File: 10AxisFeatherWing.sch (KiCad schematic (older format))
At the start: 24 parts, among them J1 feather long, J2 feather short, J3 INT, J4 feather long, J5 feather short, SW1 SW_Push_Dual, U1 BNO055, U2 BME280, Y1 32.768kHz

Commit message: Updated features
Replaced NRESET with pin instead of a button, Added silk text
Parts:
- removed R3: 10K, Resistor_SMD:R_0603_1608Metric, symbol Device:R_Small
- removed SW1: SW_Push_Dual, Button_Switch_SMD:SW_Push_1P1T_NO_CK_KMR2, symbol Switch:SW_Push_Dual
- added J6: NRESET, Connector_Wire:SolderWirePad_1x01_Drill0.8mm, symbol Connector_Generic:Conn_01x01
- J3: renamed from J4; footprint Connector_PinHeader_2.54mm:PinHeader_1x16_P2.54mm_Vertical -> Connector_PinSocket_2.54mm:PinSocket_1x16_P2.54mm_Vertical
- J4: renamed from J5; footprint Connector_PinHeader_2.54mm:PinHeader_1x12_P2.54mm_Vertical -> Connector_PinSocket_2.54mm:PinSocket_1x12_P2.54mm_Vertical
- J5: renamed from J3; footprint Connector_PinSocket_1.27mm:PinSocket_1x01_P1.27mm_Vertical -> Connector_Wire:SolderWirePad_1x01_Drill0.8mm
- renumbered C4 to C1, C5 to C2, C6 to C3, C7 to C4, C8 to C5, C2 to C6, C1 to C7, C3 to C8, R4 to R3, R5 to R4
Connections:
- net NRESET: now also J6.1 (Pin_1)
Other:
- moved on the sheet: J5, R1, R2

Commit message: Minor format fix
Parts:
- added H1, H2, H3, H4: MountingHole, MountingHole:MountingHole_2.7mm_M2.5, symbol Mechanical:MountingHole
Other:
- moved on the sheet: J5, J6
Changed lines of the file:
@@
 L Connector_Generic:Conn_01x01 J5
 U 1 1 5E233B4E
-P 10000 5500
-F 0 "J5" H 10080 5542 50  0000 L CNN
-F 1 "INT" H 10080 5451 50  0000 L CNN
-F 2 "Connector_Wire:SolderWirePad_1x01_Drill0.8mm" H 10000 5500 50  0001 C CNN
-F 3 "~" H 10000 5500 50  0001 C CNN
-	1    10000 5500
+P 10000 4800
+F 0 "J5" H 10080 4842 50  0000 L CNN
+F 1 "INT" H 10080 4751 50  0000 L CNN
+F 2 "Connector_Wire:SolderWirePad_1x01_Drill0.8mm" H 10000 4800 50  0001 C CNN
+F 3 "~" H 10000 4800 50  0001 C CNN
+	1    10000 4800
 	1    0    0    -1
 $EndComp
-Text Label 9000 5500 0    50   ~ 0
+Text Label 9000 4800 0    50   ~ 0
 INT
 Wire Wire Line
@@
 Wire Notes Line
 	6200 500  6200 8000
-Text Label 9000 6000 0    50   ~ 0
+Text Label 9000 5300 0    50   ~ 0
 NRESET
 $Comp
 L Connector_Generic:Conn_01x01 J6
 U 1 1 5E15A9A2
-P 10000 6000
-F 0 "J6" H 10080 6042 50  0000 L CNN
-F 1 "NRESET" H 10080 5951 50  0000 L CNN
-F 2 "Connector_Wire:SolderWirePad_1x01_Drill0.8mm" H 10000 6000 50  0001 C CNN
-F 3 "~" H 10000 6000 50  0001 C CNN
-	1    10000 6000
+P 10000 5300
+F 0 "J6" H 10080 5342 50  0000 L CNN
+F 1 "NRESET" H 10080 5251 50  0000 L CNN
+F 2 "Connector_Wire:SolderWirePad_1x01_Drill0.8mm" H 10000 5300 50  0001 C CNN
+F 3 "~" H 10000 5300 50  0001 C CNN
+	1    10000 5300
 	1    0    0    -1
 $EndComp
 Wire Wire Line
-	9000 5500 9800 5500
+	9000 4800 9800 4800
 Wire Wire Line
-	9000 6000 9800 6000
+	9000 5300 9800 5300
 Wire Wire Line
 	6500 2000 7750 2000
@@
 Wire Wire Line
 	7250 1500 7250 1350
+$Comp
+L Mechanical:MountingHole H1
+U 1 1 5E165FBB
+P 9250 5750
+F 0 "H1" H 9350 5796 50  0000 L CNN
+F 1 "MountingHole" H 9350 5705 50  0000 L CNN
+F 2 "MountingHole:MountingHole_2.7mm_M2.5" H 9250 5750 50  0001 C CNN
+F 3 "~" H 9250 5750 50  0001 C CNN
+	1    9250 5750
+	1    0    0    -1
+$EndComp
+$Comp
+L Mechanical:MountingHole H2
+U 1 1 5E16676B
+P 9250 6000
+F 0 "H2" H 9350 6046 50  0000 L CNN
+F 1 "MountingHole" H 9350 5955 50  0000 L CNN
+F 2 "MountingHole:MountingHole_2.7mm_M2.5" H 9250 6000 50  0001 C CNN
+F 3 "~" H 9250 6000 50  0001 C CNN
+	1    9250 6000
+	1    0    0    -1
+$EndComp
+$Comp
+L Mechanical:MountingHole H3
+U 1 1 5E166D96
+P 9250 6250
+F 0 "H3" H 9350 6296 50  0000 L CNN
+F 1 "MountingHole" H 9350 6205 50  0000 L CNN
+F 2 "MountingHole:MountingHole_2.7mm_M2.5" H 9250 6250 50  0001 C CNN
+F 3 "~" H 9250 6250 50  0001 C CNN
+	1    9250 6250
+	1    0    0    -1
+$EndComp
+$Comp
+L Mechanical:MountingHole H4
+U 1 1 5E16742A
+P 9250 6500
+F 0 "H4" H 9350 6546 50  0000 L CNN
+F 1 "MountingHole" H 9350 6455 50  0000 L CNN
+F 2 "MountingHole:MountingHole_2.7mm_M2.5" H 9250 6500 50  0001 C CNN
+F 3 "~" H 9250 6500 50  0001 C CNN
+	1    9250 6500
+	1    0    0    -1
+$EndComp
+Wire Notes Line
+	8350 5500 10500 5500
 $EndSCHEMATC

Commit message: Increased trace width
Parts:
- added R3: 10K, Resistor_SMD:R_0603_1608Metric, symbol Device:R_Small
- renumbered R3 to R4, R4 to R5
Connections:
- net +3V3: now also R3.1
- net NRESET: now also R3.2
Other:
- moved on the sheet: R2
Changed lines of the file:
@@
 $EndComp
 $Comp
-L power:GND #PWR06
+L power:GND #PWR07
 U 1 1 5D3787E4
 P 8550 1300
-F 0 "#PWR06" H 8550 1050 50  0001 C CNN
+F 0 "#PWR07" H 8550 1050 50  0001 C CNN
 F 1 "GND" H 8555 1127 50  0000 C CNN
 F 2 "" H 8550 1300 50  0001 C CNN
@@
 $EndComp
 $Comp
-L power:+3.3V #PWR04
+L power:+3.3V #PWR05
 U 1 1 5E0B811E
 P 2900 1150
-F 0 "#PWR04" H 2900 1000 50  0001 C CNN
+F 0 "#PWR05" H 2900 1000 50  0001 C CNN
 F 1 "+3.3V" H 2915 1323 50  0000 C CNN
 F 2 "" H 2900 1150 50  0001 C CNN
@@
 $EndComp
 $Comp
-L power:+3.3V #PWR05
+L power:+3.3V #PWR06
 U 1 1 5E0B916F
 P 3100 1150
-F 0 "#PWR05" H 3100 1000 50  0001 C CNN
+F 0 "#PWR06" H 3100 1000 50  0001 C CNN
 F 1 "+3.3V" H 3115 1323 50  0000 C CNN
 F 2 "" H 3100 1150 50  0001 C CNN
@@
 $EndComp
 $Comp
-L power:GND #PWR010
+L power:GND #PWR011
 U 1 1 5E0B93DE
 P 3000 3900
-F 0 "#PWR010" H 3000 3650 50  0001 C CNN
+F 0 "#PWR011" H 3000 3650 50  0001 C CNN
 F 1 "GND" H 3005 3727 50  0000 C CNN
 F 2 "" H 3000 3900 50  0001 C CNN
@@
 	4500 3300 4500 3400
 $Comp
-L power:+3.3V #PWR013
+L power:+3.3V #PWR014
 U 1 1 5E0F5D23
 P 2900 5250
-F 0 "#PWR013" H 2900 5100 50  0001 C CNN
+F 0 "#PWR014" H 2900 5100 50  0001 C CNN
 F 1 "+3.3V" H 2915 5423 50  0000 C CNN
 F 2 "" H 2900 5250 50  0001 C CNN
@@
 $EndComp
 $Comp
-L power:+3.3V #PWR014
+L power:+3.3V #PWR015
 U 1 1 5E0F8609
 P 3100 5250
-F 0 "#PWR014" H 3100 5100 50  0001 C CNN
+F 0 "#PWR015" H 3100 5100 50  0001 C CNN
 F 1 "+3.3V" H 3115 5423 50  0000 C CNN
 F 2 "" H 3100 5250 50  0001 C CNN
@@
 $EndComp
 $Comp
-L power:GND #PWR016
+L power:GND #PWR017
 U 1 1 5E0F88FA
 P 3000 7150
-F 0 "#PWR016" H 3000 6900 50  0001 C CNN
+F 0 "#PWR017" H 3000 6900 50  0001 C CNN
 F 1 "GND" H 3005 6977 50  0000 C CNN
 F 2 "" H 3000 7150 50  0001 C CNN
@@
 	9700 4450 9950 4450
 $Comp
-L power:+3.3V #PWR07
+L power:+3.3V #PWR08
 U 1 1 5E16B6E2
 P 8550 2950
-F 0 "#PWR07" H 8550 2800 50  0001 C CNN
+F 0 "#PWR08" H 8550 2800 50  0001 C CNN
 F 1 "+3.3V" H 8565 3123 50  0000 C CNN
 F 2 "" H 8550 2950 50  0001 C CNN
@@
 $EndComp
 $Comp
-L power:GND #PWR09
+L power:GND #PWR010
 U 1 1 5E16B6EC
 P 8550 3350
-F 0 "#PWR09" H 8550 3100 50  0001 C CNN
+F 0 "#PWR010" H 8550 3100 50  0001 C CNN
 F 1 "GND" H 8555 3177 50  0000 C CNN
 F 2 "" H 8550 3350 50  0001 C CNN
@@
 L Device:R_Small R2
 U 1 1 5E1917EB
-P 7750 1250
-F 0 "R2" H 7809 1296 50  0000 L CNN
-F 1 "10K" H 7809 1205 50  0000 L CNN
-F 2 "Resistor_SMD:R_0603_1608Metric" H 7750 1250 50  0001 C CNN
-F 3 "~" H 7750 1250 50  0001 C CNN
-	1    7750 1250
+P 7500 1250
+F 0 "R2" H 7559 1296 50  0000 L CNN
+F 1 "10K" H 7559 1205 50  0000 L CNN
+F 2 "Resistor_SMD:R_0603_1608Metric" H 7500 1250 50  0001 C CNN
+F 3 "~" H 7500 1250 50  0001 C CNN
+	1    7500 1250
 	1    0    0    -1
 $EndComp
@@
 Text Label 6500 1500 0    50   ~ 0
 SDA
-Text Label 6500 2000 0    50   ~ 0
+Text Label 6500 1750 0    50   ~ 0
 SCL
 $Comp
@@
 L power:+3.3V #PWR03
 U 1 1 5E1FAD43
-P 7750 1050
-F 0 "#PWR03" H 7750 900 50  0001 C CNN
-F 1 "+3.3V" H 7765 1223 50  0000 C CNN
-F 2 "" H 7750 1050 50  0001 C CNN
-F 3 "" H 7750 1050 50  0001 C CNN
-	1    7750 1050
+P 7500 1050
+F 0 "#PWR03" H 7500 900 50  0001 C CNN
+F 1 "+3.3V" H 7515 1223 50  0000 C CNN
+F 2 "" H 7500 1050 50  0001 C CNN
+F 3 "" H 7500 1050 50  0001 C CNN
+	1    7500 1050
 	1    0    0    -1
 $EndComp
@@
 	7250 1150 7250 1050
 Wire Wire Line
-	7750 1150 7750 1050
+	7500 1150 7500 1050
 $Comp
 L Jumper:SolderJumper_2_Open JP1
@@
 $EndComp
 $Comp
-L Device:R_Small R3
+L Device:R_Small R4
 U 1 1 5E22C94C
 P 7750 3750
-F 0 "R3" V 7554 3750 50  0000 C CNN
+F 0 "R4" V 7554 3750 50  0000 C CNN
 F 1 "10K" V 7645 3750 50  0000 C CNN
 F 2 "Resistor_SMD:R_0603_1608Metric" H 7750 3750 50  0001 C CNN
@@
 $EndComp
 $Comp
-L Device:R_Small R4
+L Device:R_Small R5
 U 1 1 5E22CD6F
 P 7750 5750
-F 0 "R4" V 7554 5750 50  0000 C CNN
+F 0 "R5" V 7554 5750 50  0000 C CNN
 F 1 "10K" V 7645 5750 50  0000 C CNN
 F 2 "Resistor_SMD:R_0603_1608Metric" H 7750 5750 50  0001 C CNN
@@
 	7250 3750 7650 3750
 $Comp
-L power:+3.3V #PWR08
+L power:+3.3V #PWR09
 U 1 1 5E248530
 P 7250 3000
-F 0 "#PWR08" H 7250 2850 50  0001 C CNN
+F 0 "#PWR09" H 7250 2850 50  0001 C CNN
 F 1 "+3.3V" H 7265 3173 50  0000 C CNN
 F 2 "" H 7250 3000 50  0001 C CNN
@@
 $EndComp
 $Comp
-L power:+3.3V #PWR012
+L power:+3.3V #PWR013
 U 1 1 5E248952
 P 7250 5000
-F 0 "#PWR012" H 7250 4850 50  0001 C CNN
+F 0 "#PWR013" H 7250 4850 50  0001 C CNN
 F 1 "+3.3V" H 7265 5173 50  0000 C CNN
 F 2 "" H 7250 5000 50  0001 C CNN
@@
 	7250 5750 7650 5750
 $Comp
-L power:GND #PWR011
+L power:GND #PWR012
 U 1 1 5E263677
 P 8000 4000
-F 0 "#PWR011" H 8000 3750 50  0001 C CNN
+F 0 "#PWR012" H 8000 3750 50  0001 C CNN
 F 1 "GND" H 8005 3827 50  0000 C CNN
 F 2 "" H 8000 4000 50  0001 C CNN
@@
 $EndComp
 $Comp
-L power:GND #PWR015
+L power:GND #PWR016
 U 1 1 5E263AA5
 P 8000 6000
-F 0 "#PWR015" H 8000 5750 50  0001 C CNN
+F 0 "#PWR016" H 8000 5750 50  0001 C CNN
 F 1 "GND" H 8005 5827 50  0000 C CNN
 F 2 "" H 8000 6000 50  0001 C CNN
@@
 	9000 5300 9800 5300
 Wire Wire Line
-	6500 2000 7750 2000
-Wire Wire Line
-	7750 2000 7750 1350
+	6500 1750 7500 1750
 Wire Wire Line
 	6500 1500 7250 1500
@@
 Wire Notes Line
 	8350 5500 10500 5500
+Wire Wire Line
+	7500 1750 7500 1350
+$Comp
+L Device:R_Small R3
+U 1 1 5E1C1A5F
+P 7750 1250
+F 0 "R3" H 7809 1296 50  0000 L CNN
+F 1 "10K" H 7809 1205 50  0000 L CNN
+F 2 "Resistor_SMD:R_0603_1608Metric" H 7750 1250 50  0001 C CNN
+F 3 "~" H 7750 1250 50  0001 C CNN
+	1    7750 1250
+	1    0    0    -1
+$EndComp
+$Comp
+L power:+3.3V #PWR04
+U 1 1 5E1C1A69
+P 7750 1050
+F 0 "#PWR04" H 7750 900 50  0001 C CNN
+F 1 "+3.3V" H 7765 1223 50  0000 C CNN
+F 2 "" H 7750 1050 50  0001 C CNN
+F 3 "" H 7750 1050 50  0001 C CNN
+	1    7750 1050
+	1    0    0    -1
+$EndComp
+Wire Wire Line
+	7750 1150 7750 1050
+Text Label 6500 2000 0    50   ~ 0
+NRESET
+Wire Wire Line
+	6500 2000 7750 2000
+Wire Wire Line
+	7750 1350 7750 2000
 $EndSCHEMATC

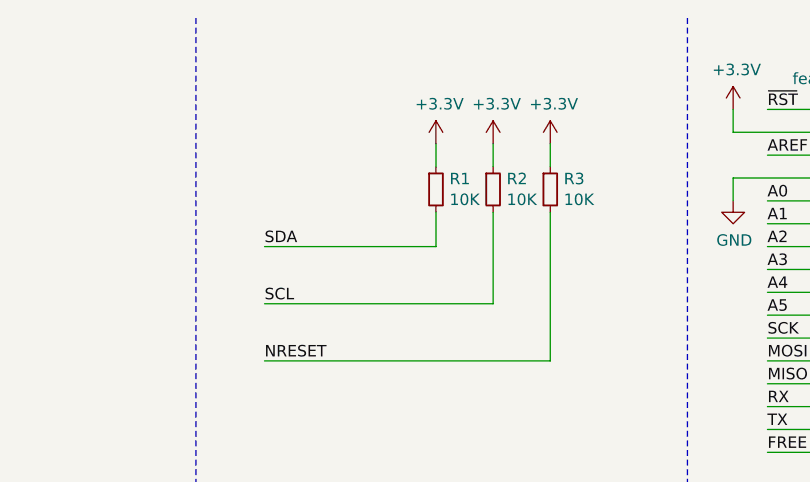
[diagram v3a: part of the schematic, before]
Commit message: I2C pull-up resistor fix
Changed I2C pull-up resistor values from 10K to 4.7K
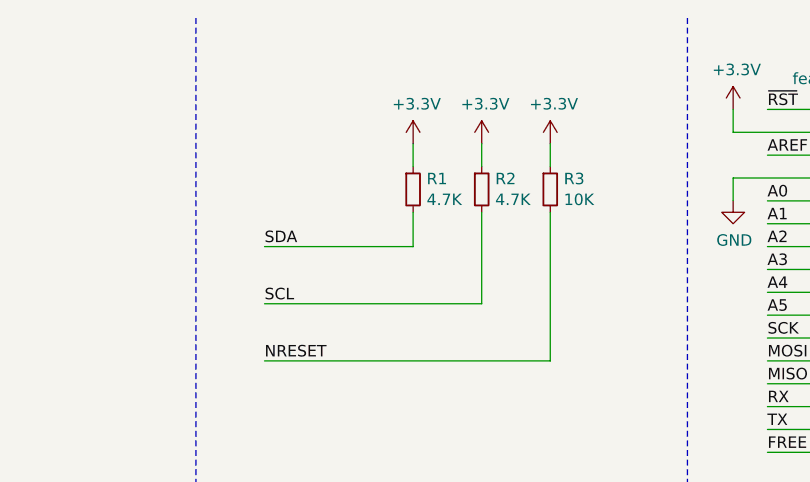
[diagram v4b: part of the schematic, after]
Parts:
- R1, R2: value 10K -> 4.7K
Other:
- moved on the sheet: R1, R2
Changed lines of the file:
@@
 	8350 500  8350 6650
-$Comp
-L Device:R_Small R1
-U 1 1 5E19106A
-P 7250 1250
-F 0 "R1" H 7309 1296 50  0000 L CNN
-F 1 "10K" H 7309 1205 50  0000 L CNN
-F 2 "Resistor_SMD:R_0603_1608Metric" H 7250 1250 50  0001 C CNN
-F 3 "~" H 7250 1250 50  0001 C CNN
-	1    7250 1250
-	1    0    0    -1
-$EndComp
 $Comp
 L Device:R_Small R2
 U 1 1 5E1917EB
-P 7500 1250
-F 0 "R2" H 7559 1296 50  0000 L CNN
-F 1 "10K" H 7559 1205 50  0000 L CNN
-F 2 "Resistor_SMD:R_0603_1608Metric" H 7500 1250 50  0001 C CNN
-F 3 "~" H 7500 1250 50  0001 C CNN
-	1    7500 1250
+P 7450 1250
+F 0 "R2" H 7509 1296 50  0000 L CNN
+F 1 "4.7K" H 7509 1205 50  0000 L CNN
+F 2 "Resistor_SMD:R_0603_1608Metric" H 7450 1250 50  0001 C CNN
+F 3 "~" H 7450 1250 50  0001 C CNN
+	1    7450 1250
 	1    0    0    -1
 $EndComp
@@
 Wire Notes Line
 	6200 6650 10500 6650
-Text Label 6500 1500 0    50   ~ 0
-SDA
 Text Label 6500 1750 0    50   ~ 0
 SCL
@@
 L power:+3.3V #PWR02
 U 1 1 5E1FA9BB
-P 7250 1050
-F 0 "#PWR02" H 7250 900 50  0001 C CNN
-F 1 "+3.3V" H 7265 1223 50  0000 C CNN
-F 2 "" H 7250 1050 50  0001 C CNN
-F 3 "" H 7250 1050 50  0001 C CNN
-	1    7250 1050
+P 7150 1050
+F 0 "#PWR02" H 7150 900 50  0001 C CNN
+F 1 "+3.3V" H 7165 1223 50  0000 C CNN
+F 2 "" H 7150 1050 50  0001 C CNN
+F 3 "" H 7150 1050 50  0001 C CNN
+	1    7150 1050
 	1    0    0    -1
 $EndComp
@@
 L power:+3.3V #PWR03
 U 1 1 5E1FAD43
-P 7500 1050
-F 0 "#PWR03" H 7500 900 50  0001 C CNN
-F 1 "+3.3V" H 7515 1223 50  0000 C CNN
-F 2 "" H 7500 1050 50  0001 C CNN
-F 3 "" H 7500 1050 50  0001 C CNN
-	1    7500 1050
-	1    0    0    -1
-$EndComp
-Wire Wire Line
-	7250 1150 7250 1050
-Wire Wire Line
-	7500 1150 7500 1050
+P 7450 1050
+F 0 "#PWR03" H 7450 900 50  0001 C CNN
+F 1 "+3.3V" H 7465 1223 50  0000 C CNN
+F 2 "" H 7450 1050 50  0001 C CNN
+F 3 "" H 7450 1050 50  0001 C CNN
+	1    7450 1050
+	1    0    0    -1
+$EndComp
+Wire Wire Line
+	7150 1150 7150 1050
+Wire Wire Line
+	7450 1150 7450 1050
 $Comp
 L Jumper:SolderJumper_2_Open JP1
@@
 Wire Wire Line
 	9000 5300 9800 5300
-Wire Wire Line
-	6500 1750 7500 1750
-Wire Wire Line
-	6500 1500 7250 1500
-Wire Wire Line
-	7250 1500 7250 1350
 $Comp
 L Mechanical:MountingHole H1
@@
 	8350 5500 10500 5500
 Wire Wire Line
-	7500 1750 7500 1350
+	7450 1750 7450 1350
 $Comp
 L Device:R_Small R3
@@
 Wire Wire Line
 	7750 1350 7750 2000
+Text Label 6500 1500 0    50   ~ 0
+SDA
+$Comp
+L Device:R_Small R1
+U 1 1 5E19106A
+P 7150 1250
+F 0 "R1" H 7209 1296 50  0000 L CNN
+F 1 "4.7K" H 7209 1205 50  0000 L CNN
+F 2 "Resistor_SMD:R_0603_1608Metric" H 7150 1250 50  0001 C CNN
+F 3 "~" H 7150 1250 50  0001 C CNN
+	1    7150 1250
+	1    0    0    -1
+$EndComp
+Wire Wire Line
+	7150 1350 7150 1500
+Wire Wire Line
+	6500 1750 7450 1750
+Wire Wire Line
+	6500 1500 7150 1500
 $EndSCHEMATC
